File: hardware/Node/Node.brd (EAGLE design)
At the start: 49.5 x 49.5 mm, 71 parts, among them J1 AVR_SPI_PRG_6NS, J2 M04X2, Q1 PMR280UN, Q2 PMR280UN, Q3 PMR280UN, SW1 KSS, SW2 KSS, U1 ATMEGA32U4QFN, U2 BLUETOOTH-RN41", U3 LSM303DLM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

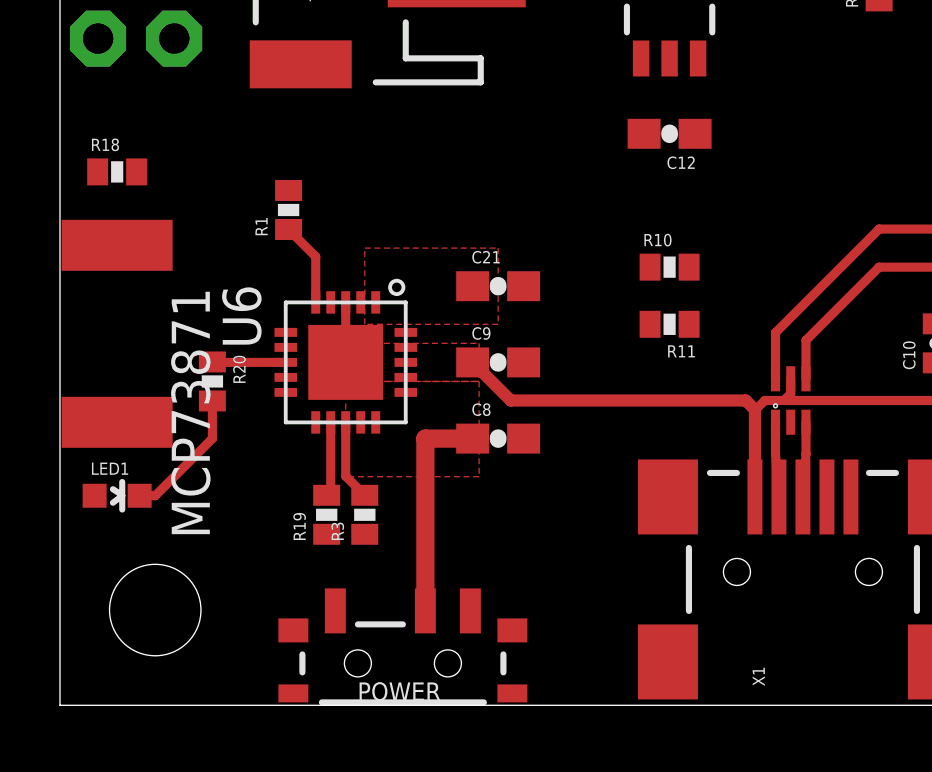
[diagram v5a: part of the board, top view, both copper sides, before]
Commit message: route low battery led
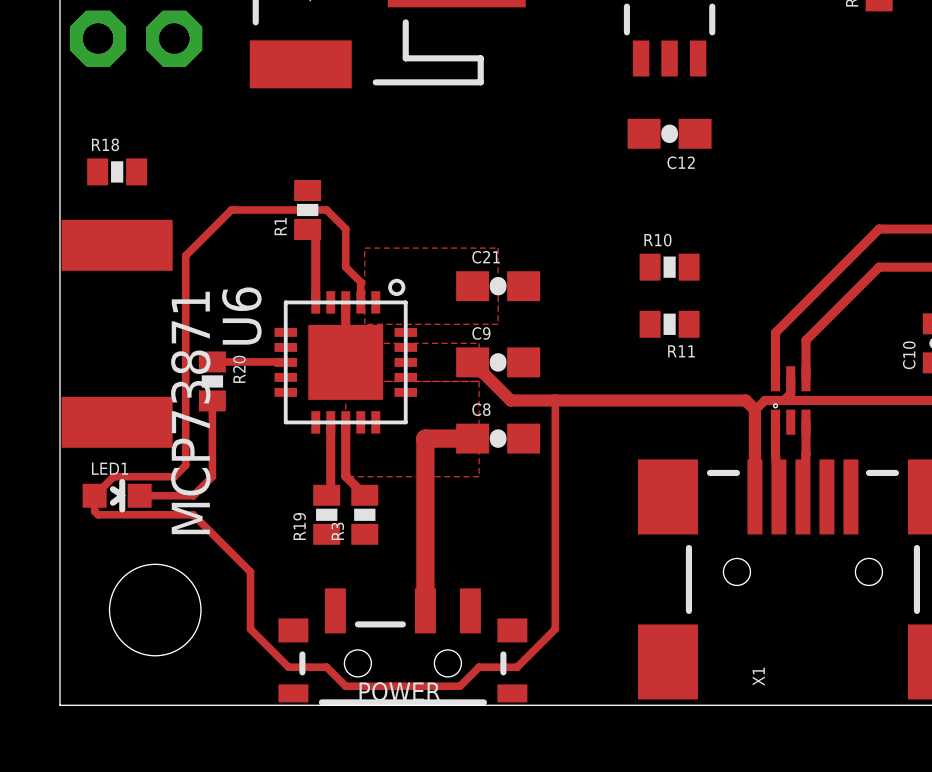
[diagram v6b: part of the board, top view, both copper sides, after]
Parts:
- moved R1 0.64 mm to (8.26, 16.5)
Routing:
- net VBUS: track 25.0 -> 72.2 mm
- net N$13: track 4.47 -> 5.21 mm
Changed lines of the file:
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@@
 <wire x1="49.53" y1="49.53" x2="0" y2="49.53" width="0" layer="20"/>
 <wire x1="0" y1="49.53" x2="0" y2="0" width="0" layer="20"/>
+<rectangle x1="6.985" y1="34.29" x2="15.875" y2="48.26" layer="39"/>
+<rectangle x1="6.985" y1="34.29" x2="15.875" y2="48.26" layer="41"/>
+<rectangle x1="6.985" y1="34.29" x2="15.875" y2="48.26" layer="40"/>
+<rectangle x1="6.985" y1="34.29" x2="15.875" y2="48.26" layer="42"/>
 </plain>
 <attributes>
@@
 <element name="C8" library="SparkFun" package="0603-CAP" value="4.7uF" x="14.605" y="8.89"/>
 <element name="C21" library="SparkFun" package="0603-CAP" value="4.7uF" x="14.605" y="13.97"/>
-<element name="R1" library="SparkFun" package="0402-RES" value="10k" x="7.62" y="16.51" rot="R90"/>
+<element name="R1" library="SparkFun" package="0402-RES" value="10k" x="8.255" y="16.51" rot="R90"/>
 <element name="R3" library="SparkFun" package="0402-RES" value="2k" x="10.16" y="6.35" rot="R90"/>
 <element name="R19" library="SparkFun" package="0402-RES" value="100k" x="8.89" y="6.35" rot="R90"/>
@@
 <wire x1="8.89" y1="5.7" x2="8.525" y2="9.43" width="0" layer="19" extent="1-1"/>
 <wire x1="10.16" y1="5.7" x2="8.89" y2="5.7" width="0" layer="19" extent="1-1"/>
-<wire x1="7.62" y1="17.16" x2="9.525" y2="13.43" width="0" layer="19" extent="1-1"/>
-<wire x1="1.905" y1="15.3325" x2="7.62" y2="17.16" width="0" layer="19" extent="1-1"/>
-<wire x1="3.81" y1="22.225" x2="7.62" y2="17.16" width="0" layer="19" extent="1-1"/>
+<wire x1="8.255" y1="17.16" x2="9.525" y2="13.43" width="0" layer="19" extent="1-1"/>
+<wire x1="1.905" y1="15.3325" x2="8.255" y2="17.16" width="0" layer="19" extent="1-1"/>
+<wire x1="3.81" y1="22.225" x2="8.255" y2="17.16" width="0" layer="19" extent="1-1"/>
 <wire x1="13.225" y1="25.765" x2="21.17" y2="26.67" width="0" layer="19" extent="1-1"/>
 <wire x1="48.26" y1="28.575" x2="40.005" y2="26.25" width="0" layer="19" extent="1-1"/>
@@
 <contactref element="U3" pad="20"/>
 <contactref element="U4" pad="2"/>
-<wire x1="36.11" y1="28.97" x2="38.115" y2="40.64" width="0" layer="19" extent="1-1"/>
-<wire x1="37.33" y1="9.3" x2="37.86" y2="27.77" width="0" layer="19" extent="1-1"/>
 <wire x1="40.06" y1="40.33" x2="38.41" y2="40.33" width="0.254" layer="1"/>
 <wire x1="38.41" y1="40.33" x2="38.1" y2="40.64" width="0.254" layer="1"/>
-<wire x1="38.1" y1="40.64" x2="38.115" y2="40.64" width="0" layer="19" extent="1-16"/>
 <wire x1="37.86" y1="27.77" x2="36.365" y2="27.77" width="0.254" layer="1"/>
 <wire x1="36.365" y1="27.77" x2="36.11" y2="28.025" width="0.254" layer="1"/>
 <wire x1="36.11" y1="28.025" x2="36.11" y2="28.97" width="0.254" layer="1"/>
+<wire x1="38.1" y1="40.64" x2="38.115" y2="40.64" width="0" layer="19" extent="1-1"/>
+<wire x1="36.11" y1="28.97" x2="38.41" y2="40.33" width="0" layer="19" extent="1-1"/>
+<wire x1="37.33" y1="9.3" x2="37.86" y2="27.77" width="0" layer="19" extent="1-1"/>
 </signal>
 <signal name="SDA">
@@
 <contactref element="U1" pad="19"/>
 <contactref element="R16" pad="1"/>
-<wire x1="35.56" y1="28.97" x2="38.115" y2="39.37" width="0" layer="19" extent="1-1"/>
-<wire x1="37.83" y1="9.3" x2="37.86" y2="27.22" width="0" layer="19" extent="1-1"/>
 <wire x1="40.06" y1="39.68" x2="38.425" y2="39.68" width="0.254" layer="1"/>
 <wire x1="38.425" y1="39.68" x2="38.115" y2="39.37" width="0.254" layer="1"/>
@@
 <wire x1="36.28" y1="27.22" x2="35.56" y2="27.94" width="0.254" layer="1"/>
 <wire x1="35.56" y1="27.94" x2="35.56" y2="28.97" width="0.254" layer="1"/>
+<wire x1="35.56" y1="28.97" x2="38.115" y2="39.37" width="0" layer="19" extent="1-1"/>
+<wire x1="37.83" y1="9.3" x2="37.86" y2="27.22" width="0" layer="19" extent="1-1"/>
 </signal>
 <signal name="PCINT4">
@@
 <wire x1="23.165" y1="6.945" x2="23.165" y2="9.855" width="0.4064" layer="1"/>
 <wire x1="23.165" y1="9.855" x2="22.86" y2="10.16" width="0.4064" layer="1"/>
-<wire x1="22.86" y1="10.16" x2="15.025" y2="10.16" width="0.4064" layer="1"/>
+<wire x1="22.86" y1="10.16" x2="16.51" y2="10.16" width="0.4064" layer="1"/>
+<wire x1="16.51" y1="10.16" x2="15.025" y2="10.16" width="0.4064" layer="1"/>
 <wire x1="15.025" y1="10.16" x2="13.755" y2="11.43" width="0.4064" layer="1"/>
 <wire x1="31.115" y1="11.215" x2="31.33" y2="11.43" width="0.254" layer="1"/>
@@
 <wire x1="31.115" y1="11.215" x2="30.06" y2="10.16" width="0.3048" layer="1"/>
 <wire x1="30.06" y1="10.16" x2="24.13" y2="10.16" width="0.3048" layer="1"/>
-<wire x1="10.025" y1="13.43" x2="17.78" y2="41.91" width="0" layer="19" extent="1-1"/>
-<wire x1="11.525" y1="11.93" x2="10.025" y2="13.43" width="0" layer="19" extent="1-1"/>
-<wire x1="1.155" y1="6.985" x2="10.025" y2="13.43" width="0" layer="19" extent="1-1"/>
+<wire x1="1.155" y1="6.985" x2="1.155" y2="6.465" width="0.254" layer="1"/>
+<wire x1="1.155" y1="6.465" x2="1.27" y2="6.35" width="0.254" layer="1"/>
+<wire x1="1.27" y1="6.35" x2="4.445" y2="6.35" width="0.254" layer="1"/>
+<wire x1="4.445" y1="6.35" x2="6.35" y2="4.445" width="0.254" layer="1"/>
+<wire x1="6.35" y1="4.445" x2="6.35" y2="2.54" width="0.254" layer="1"/>
+<wire x1="6.35" y1="2.54" x2="7.62" y2="1.27" width="0.254" layer="1"/>
+<wire x1="7.62" y1="1.27" x2="8.89" y2="1.27" width="0.254" layer="1"/>
+<wire x1="8.89" y1="1.27" x2="9.525" y2="0.635" width="0.254" layer="1"/>
+<wire x1="9.525" y1="0.635" x2="13.335" y2="0.635" width="0.254" layer="1"/>
+<wire x1="13.335" y1="0.635" x2="13.97" y2="1.27" width="0.254" layer="1"/>
+<wire x1="13.97" y1="1.27" x2="15.24" y2="1.27" width="0.254" layer="1"/>
+<wire x1="15.24" y1="1.27" x2="16.51" y2="2.54" width="0.254" layer="1"/>
+<wire x1="16.51" y1="2.54" x2="16.51" y2="10.16" width="0.254" layer="1"/>
+<wire x1="10.025" y1="13.43" x2="10.025" y2="14.105" width="0.254" layer="1"/>
+<wire x1="10.025" y1="14.105" x2="9.525" y2="14.605" width="0.254" layer="1"/>
+<wire x1="9.525" y1="14.605" x2="9.525" y2="15.875" width="0.254" layer="1"/>
+<wire x1="9.525" y1="15.875" x2="8.89" y2="16.51" width="0.254" layer="1"/>
+<wire x1="8.89" y1="16.51" x2="5.715" y2="16.51" width="0.254" layer="1"/>
+<wire x1="5.715" y1="16.51" x2="4.191" y2="14.986" width="0.254" layer="1"/>
+<wire x1="4.445" y1="8.255" x2="3.81" y2="7.62" width="0" layer="19" extent="1-16"/>
+<wire x1="3.81" y1="7.62" x2="1.79" y2="7.62" width="0.254" layer="1"/>
+<wire x1="1.79" y1="7.62" x2="1.155" y2="6.985" width="0.254" layer="1"/>
+<wire x1="8.89" y1="16.51" x2="17.78" y2="41.91" width="0" layer="19" extent="1-1"/>
+<wire x1="4.191" y1="14.986" x2="4.191" y2="8.001" width="0.254" layer="1"/>
+<wire x1="4.191" y1="8.001" x2="3.81" y2="7.62" width="0.254" layer="1"/>
+<wire x1="3.81" y1="7.62" x2="4.445" y2="8.255" width="0" layer="19" extent="1-16"/>
 </signal>
 <signal name="RX">
@@
 <contactref element="U1" pad="26"/>
 <contactref element="Q1" pad="1"/>
-<wire x1="40.23" y1="11.7" x2="24.63" y2="30.495" width="0" layer="19" extent="1-1"/>
 <wire x1="24.63" y1="30.495" x2="24.63" y2="31.6" width="0.254" layer="1"/>
 <wire x1="24.63" y1="31.6" x2="24.78" y2="31.75" width="0.254" layer="1"/>
+<wire x1="40.23" y1="11.7" x2="24.63" y2="30.495" width="0" layer="19" extent="1-1"/>
 </signal>
 <signal name="N$23">
@@
 <wire x1="33.43" y1="13.7" x2="32.02" y2="13.7" width="0.254" layer="1"/>
 <wire x1="32.02" y1="13.7" x2="31.115" y2="14.605" width="0.254" layer="1"/>
-<wire x1="31.115" y1="14.605" x2="31.13" y2="14.605" width="0" layer="19" extent="1-16"/>
+<wire x1="31.115" y1="14.605" x2="31.13" y2="14.605" width="0" layer="19" extent="1-1"/>
 </signal>
 <signal name="N$24">
@@
 <contactref element="R4" pad="2"/>
 <contactref element="U1" pad="13"/>
-<wire x1="5.7" y1="30.48" x2="34.83" y2="9.3" width="0" layer="19" extent="1-1"/>
 <wire x1="3.19" y1="31.75" x2="5.7" y2="31.75" width="0.254" layer="1"/>
 <wire x1="5.7" y1="31.75" x2="5.7" y2="30.48" width="0.254" layer="1"/>
+<wire x1="5.7" y1="30.48" x2="34.83" y2="9.3" width="0" layer="19" extent="1-1"/>
 </signal>
 <signal name="RESET">
@@
 <contactref element="R4" pad="1"/>
 <contactref element="J1" pad="5"/>
-<wire x1="1.27" y1="22.225" x2="1.905" y2="34.1975" width="0" layer="19" extent="1-1"/>
-<wire x1="1.89" y1="31.75" x2="1.27" y2="22.225" width="0" layer="19" extent="1-1"/>
+<wire x1="1.89" y1="31.75" x2="1.905" y2="34.1975" width="0" layer="19" extent="1-1"/>
+<wire x1="1.27" y1="22.225" x2="1.89" y2="31.75" width="0" layer="19" extent="1-1"/>
 </signal>
 <signal name="SCK">
@@
 <contactref element="U6" pad="5"/>
 <contactref element="R1" pad="1"/>
-<wire x1="8.525" y1="13.43" x2="8.525" y2="14.955" width="0.3048" layer="1"/>
-<wire x1="8.525" y1="14.955" x2="7.62" y2="15.86" width="0.3048" layer="1"/>
+<wire x1="8.525" y1="13.43" x2="8.525" y2="15.59" width="0.3048" layer="1"/>
+<wire x1="8.525" y1="15.59" x2="8.255" y2="15.86" width="0.3048" layer="1"/>
 </signal>
 <signal name="N$16">
@@
 <contactref element="LED1" pad="C"/>
 <contactref element="R20" pad="2"/>
-<wire x1="5.08" y1="10.145" x2="5.08" y2="8.89" width="0.3048" layer="1"/>
-<wire x1="5.08" y1="8.89" x2="3.175" y2="6.985" width="0.3048" layer="1"/>
-<wire x1="3.175" y1="6.985" x2="2.655" y2="6.985" width="0.3048" layer="1"/>
+<wire x1="2.655" y1="6.985" x2="4.445" y2="6.985" width="0.254" layer="1"/>
+<wire x1="4.445" y1="6.985" x2="5.08" y2="7.62" width="0.254" layer="1"/>
+<wire x1="5.08" y1="7.62" x2="5.08" y2="10.145" width="0.254" layer="1"/>
 </signal>
 <signal name="N$19">
 <contactref element="U6" pad="8"/>
 <contactref element="R20" pad="1"/>
-<wire x1="7.525" y1="11.43" x2="5.095" y2="11.43" width="0.3048" layer="1"/>
-<wire x1="5.095" y1="11.43" x2="5.08" y2="11.445" width="0.3048" layer="1"/>
+<wire x1="5.08" y1="11.445" x2="7.51" y2="11.445" width="0.254" layer="1"/>
+<wire x1="7.51" y1="11.445" x2="7.525" y2="11.43" width="0.254" layer="1"/>
 </signal>
 <signal name="VDIV">

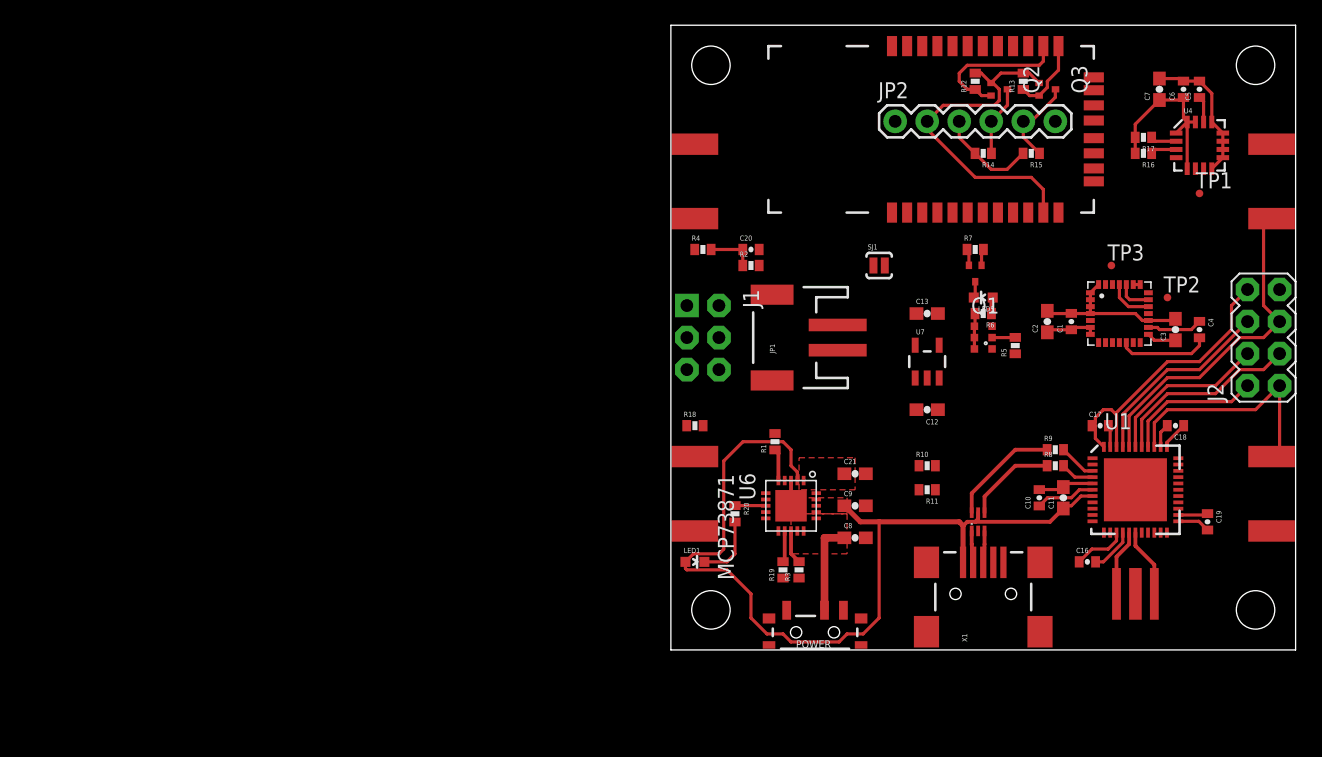
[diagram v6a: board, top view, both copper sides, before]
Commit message: move stuff to meet the DRC
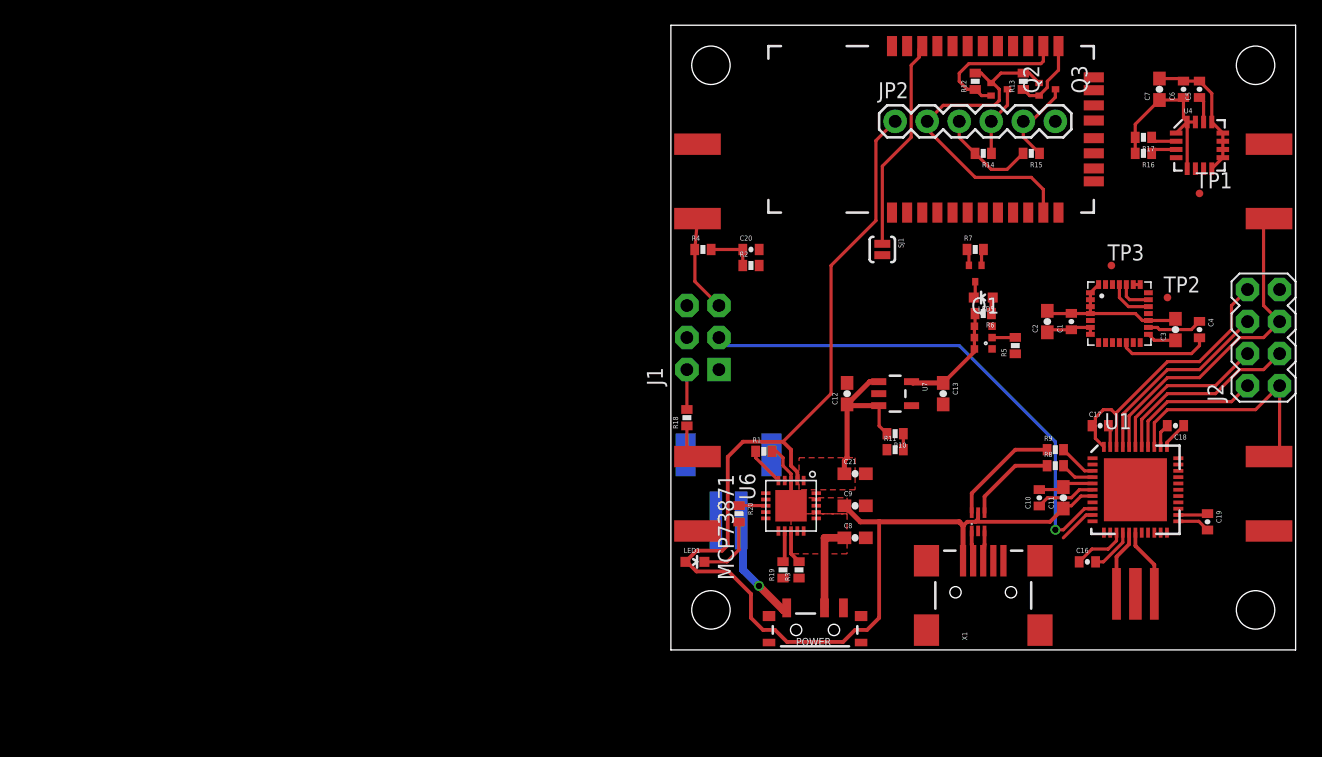
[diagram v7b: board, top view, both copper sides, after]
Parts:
- moved JP1 11.9 mm to (4.57, 14.0), flipped to the bottom, turned to 0 degrees
- moved C13 6.48 mm to (21.6, 20.3), turned to 270 degrees
- moved C12 6.48 mm to (14.0, 20.3), turned to 90 degrees
- moved R11 4.07 mm to (17.8, 15.9), turned to 0 degrees
- moved R10 3.59 mm to (17.8, 17.1), turned to 180 degrees
- moved U7 3.59 mm to (17.8, 20.3), turned to 270 degrees
- moved SJ1 1.30 mm to (16.8, 31.8), turned to 270 degrees
- moved R1 1.17 mm to (7.37, 15.7), turned to 0 degrees
- moved R18 0.90 mm to (1.27, 18.4), turned to 90 degrees
- moved R20 0.32 mm to (5.40, 10.8)
- moved SW1 0.20 mm to (47.4, 12.4)
- moved SW2 0.20 mm to (47.4, 37.1)
- moved HWB 0.20 mm to (2.11, 12.4)
- moved RESET 0.20 mm to (2.11, 37.1)
- moved POWER 0.19 mm to (11.4, 1.59)
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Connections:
- net GND: now also HWB.P$2; no longer HWB.P$1
- net HWB: now also HWB.P$1; no longer HWB.P$2
- net PROG2: now also U1.12; no longer U1.8
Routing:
- net SCK: track 0.00 -> 40.7 mm, vias 0 -> 1
- net VBUS: track 72.2 -> 100.7 mm
- net N$14: track 0.00 -> 17.0 mm
- net N$11: track 0.00 -> 13.6 mm
- net +3V3: track 86.9 -> 96.4 mm
- net N$29: track 0.00 -> 8.66 mm, vias 0 -> 1
- net RESET: track 0.00 -> 7.70 mm
- net GND: track 42.5 -> 45.8 mm
- net MOSI: track 0.00 -> 3.06 mm
- net HWB: track 0.00 -> 2.79 mm
- net VDIV: track 0.00 -> 1.27 mm
- net N$8: track 2.54 -> 3.07 mm
